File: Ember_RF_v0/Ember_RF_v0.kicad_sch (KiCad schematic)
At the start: 2 parts

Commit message: anything until test launch prep
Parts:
- added JP1: ~, microbuilder:1X20_ROUND, symbol microbuilder:HEADER-1X20ROUND
- added R1, R2, R3: ~, microbuilder:0603, symbol microbuilder:RESISTOR0603
- added R4, R5, R6, R7: 0, microbuilder:0603, symbol microbuilder:RESISTOR0603
- added U3: ~, E22-900M30S:XCVR_E22-900M30S, symbol E22-900M30S:E22-900M30S
- added X1: ~, adafruit:SMA90_DIP, symbol adafruit:SMACONNECTOR
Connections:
- net GPS_RX: now reaches U2.1 (RXD)
- net GPS_RX: now also U1.P$6 (GP4)
- net GND: now reaches U2.12 (GND), U2.3 (GND)
- net GND: now also U1.P$13 (GND), U1.P$18 (GND), U1.P$23 (GND), U1.P$28 (GND), U1.P$3 (GND), U1.P$33 (GND), U1.P$38 (GND), U1.P$8 (GND), JP1.2, R1.1, R2.1, R3.2, U3.1 (GND), U3.11 (GND), U3.12 (GND), U3.2 (GND), U3.20 (GND), U3.22 (GND), U3.3 (GND), U3.4 (GND), U3.5 (GND), X1.GND1, X1.GND2, X1.GND3, X1.GND4
- net SCL: now reaches U2.15 (I2C_SCL)
- net SCL: now also U1.P$5 (GP3), R3.1
- net SDA: now reaches U2.16 (I2C_SDA)
- net SDA: now also U1.P$4 (GP2), R2.2
- net GPS_TX: now reaches U2.2 (TXD)
- net GPS_TX: now also U1.P$7 (GP5)
- net 3v3: now reaches U2.4 (VCC)
- net 3v3: now also U1.P$36 (3V3(OUT)), U3.10 (VCC), U3.9 (VCC)
- net B2B_TX: now reaches U1.P$1 (GP0)
- net B2B_TX: now also JP1.3
- net LORA_MISO: now reaches U1.P$11 (GP8)
- net LORA_MISO: now also R4.1, U3.16 (MISO)
- net LORA_CS: now reaches U1.P$12 (GP9)
- net LORA_CS: now also R1.2, R7.1, U3.19 (NSS)
- net LORA_SCK: now reaches U1.P$14 (GP10)
- net LORA_SCK: now also R6.1, U3.18 (SCK)
- net LORA_MOSI: now reaches U1.P$15 (GP11)
- net LORA_MOSI: now also R5.1, U3.17 (MOSI)
- net LORA_BUSY: now reaches U1.P$16 (GP12)
- net LORA_BUSY: now also U3.14 (BUSY)
- net LORA_RST: now reaches U1.P$17 (GP13)
- net LORA_RST: now also U3.15 (~{RST})
- net LORA_DIO1: now reaches U1.P$19 (GP14)
- net LORA_DIO1: now also U3.13 (DIO1)
- net B2B_RX: now reaches U1.P$2 (GP1)
- net B2B_RX: now also JP1.4
- net 5V: now reaches U1.P$39 (VSYS)
- net 5V: now also JP1.1
- new net: JP1.5, R4.2
- new net: JP1.8, R7.2
- new net: U3.21 (ANT), X1.ANTENNA (ANT)
- new net: JP1.6, R5.2
- new net: JP1.7, R6.2

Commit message: all until 19 mar
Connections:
- net GPS_RESET: now reaches U2.10 (~{RESET})
- net GPS_RESET: now also U1.P$22 (GP17)
- net GPS_WAKE_UP: now reaches U2.7 (WAKE_UP)
- net GPS_WAKE_UP: now also U1.P$21 (GP16)
- net TXEN: now reaches U1.P$10 (GP7)
- net TXEN: now also U3.7 (TXEN)
- net RXEN: now reaches U1.P$9 (GP6)
- net RXEN: now also U3.6 (RXEN)
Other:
- moved on the sheet: R1

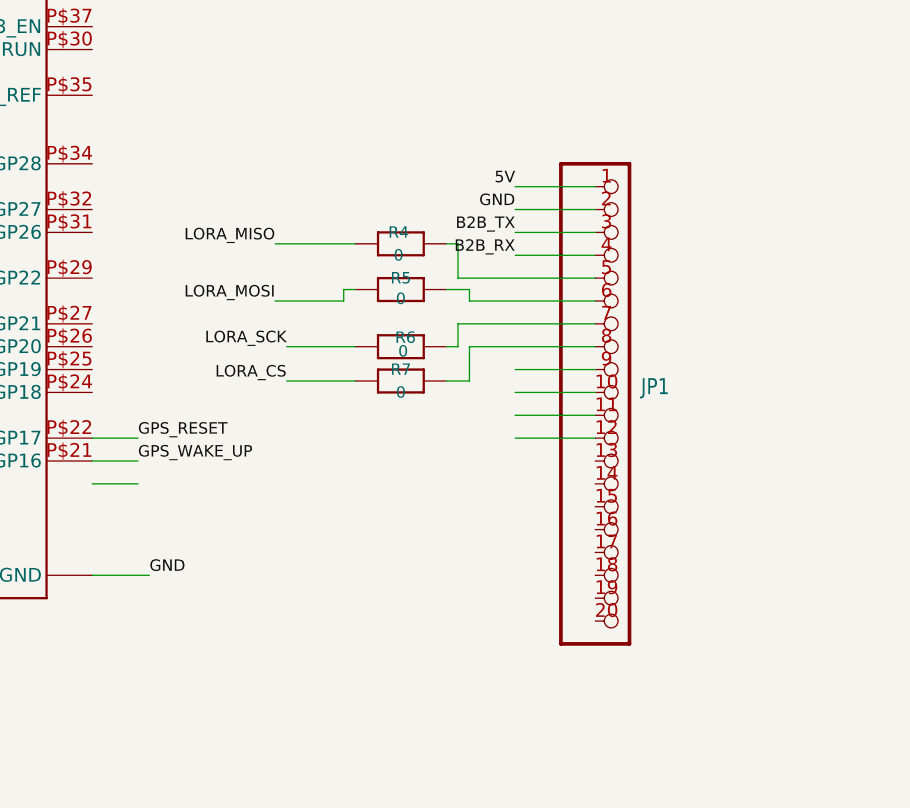
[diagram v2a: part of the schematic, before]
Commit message: Ahaan's RF Headers 16 to 4
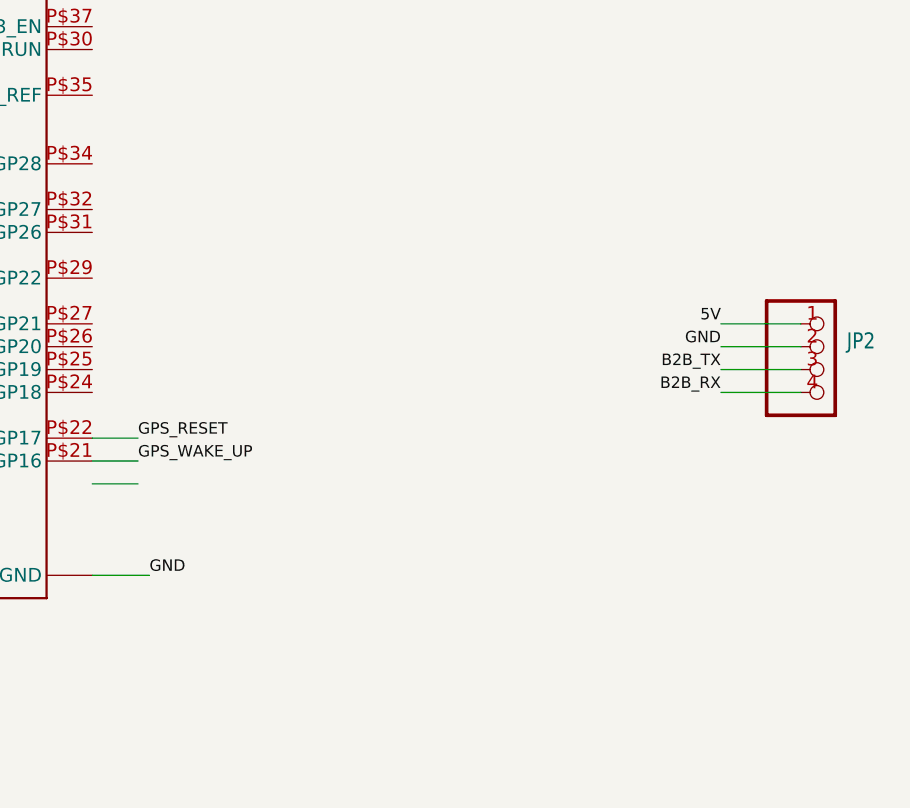
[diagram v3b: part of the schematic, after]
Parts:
- removed JP1: ~, microbuilder:1X20_ROUND, symbol microbuilder:HEADER-1X20ROUND
- removed R4, R5, R6, R7: 0, microbuilder:0603, symbol microbuilder:RESISTOR0603
- added JP2: ~, microbuilder:1X04_OVAL, symbol microbuilder:HEADER-1X4
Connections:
- net 5V: now also JP2.1
- net B2B_RX: now also JP2.4
- net B2B_TX: now also JP2.3
- net GND: now also JP2.2

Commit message: RF Board PCB Attempt 1
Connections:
- no-connect marks 1 -> 24

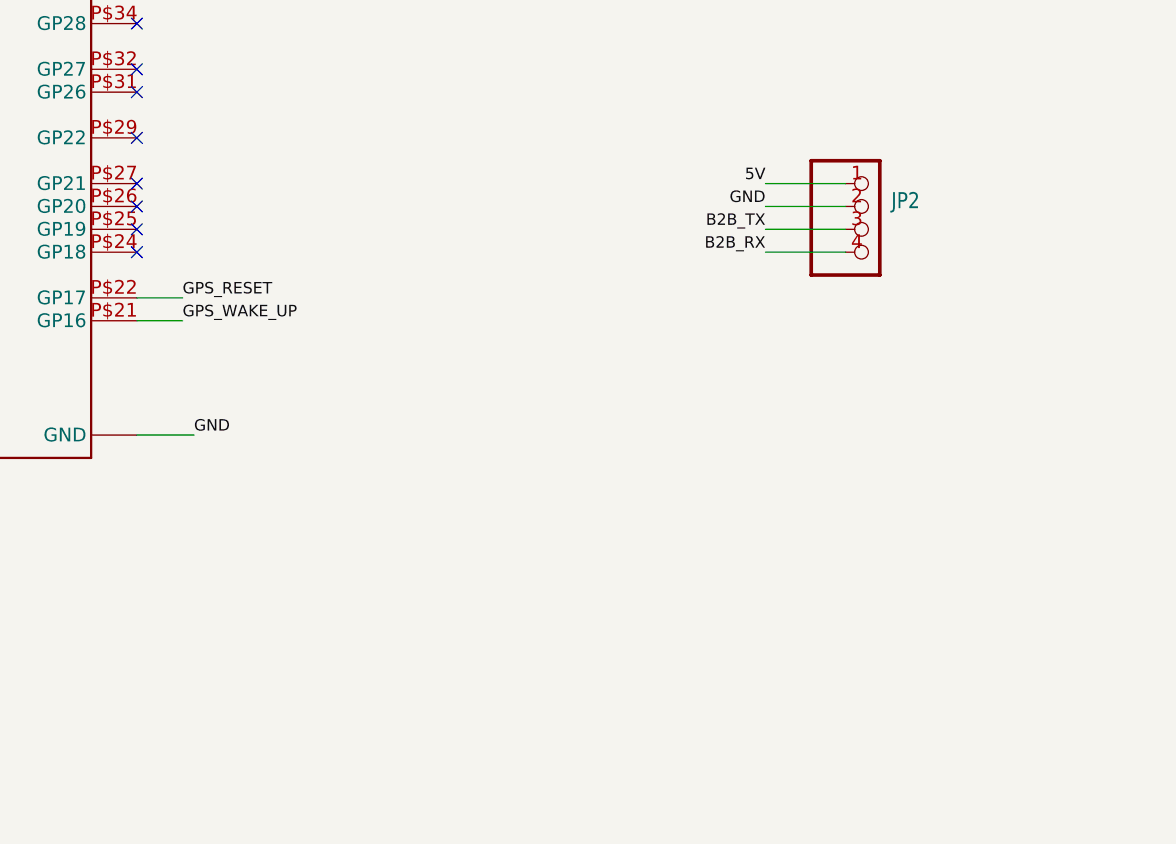
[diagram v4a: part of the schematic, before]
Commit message: Some corrections done and main board routing halfway done
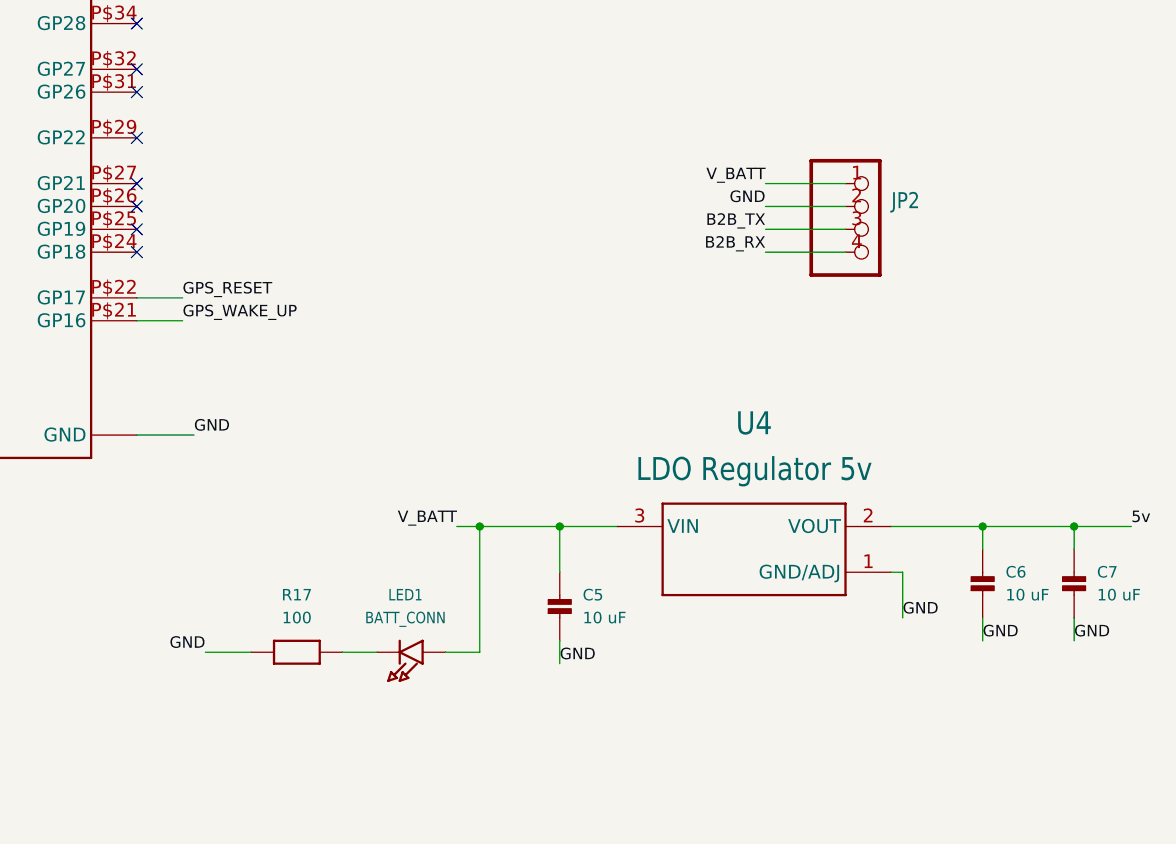
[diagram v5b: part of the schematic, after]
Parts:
- added C5, C6, C7: 10 uF, microbuilder:0603, symbol microbuilder:CAP_CERAMIC0603
- added LED1: BATT_CONN, microbuilder:CHIPLED_0603, symbol microbuilder:LED0603
- added R17: 100, microbuilder:0603, symbol microbuilder:RESISTOR0603
- added U4: LDO Regulator 5v, AMS1117-5.0:SOT229P700X180-4N, symbol AMS1117-5.0:AMS1117-5.0
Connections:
- net 5V: no longer JP2.1
- net GND: now also C5.2 (P$2), C6.2 (P$2), C7.2 (P$2), R17.1, U4.1 (GND/ADJ)
- new net: LED1.C, R17.2
- new net 5v: C6.1 (P$1), C7.1 (P$1), U4.2 (VOUT)
- new net V_BATT: C5.1 (P$1), JP2.1, LED1.A, U4.3 (VIN)

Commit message: All routings completed, Lisan Al-gaib!
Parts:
- removed X1: ~, adafruit:SMA90_DIP, symbol adafruit:SMACONNECTOR
- added J1: ~, sma-connector:RFSOLUTIONS_CON-SMA-EDGE-S, symbol sma-connector:CON-SMA-EDGE-S
- added LS2: BUZZER, CMT-8530S-SMT:CUI_CMT-8530S-SMT, symbol CMT-8530S-SMT:CMT-8530S-SMT
- added Q5: CJ3400, CJ3400:SOT95P240X115-3N, symbol CJ3400:CJ3400
- added R15: 100, microbuilder:0603, symbol microbuilder:RESISTOR0603
- added R27: 1k, microbuilder:0603, symbol microbuilder:RESISTOR0603
- added R4: 33k, microbuilder:0603, symbol microbuilder:RESISTOR0603
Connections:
- net 5V is gone; now on net 5v: U1.P$39 (VSYS)
- net 5v: now also Q5.3 (D)
- net GND: now also J1.G1 (2), J1.G2 (2), J1.G3 (2), J1.G4 (2), R15.2, R4.2
- net at U3.21 (ANT): now also J1.1
- net BUZZER: now reaches U1.P$24 (GP18)
- net BUZZER: now also R27.1
- new net: Q5.1 (G), R27.2, R4.1
- new net: LS2.P, Q5.2 (S)
- new net: LS2.N, R15.1
- no-connect marks 24 -> 23
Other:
- moved on the sheet: R2, R3, U2

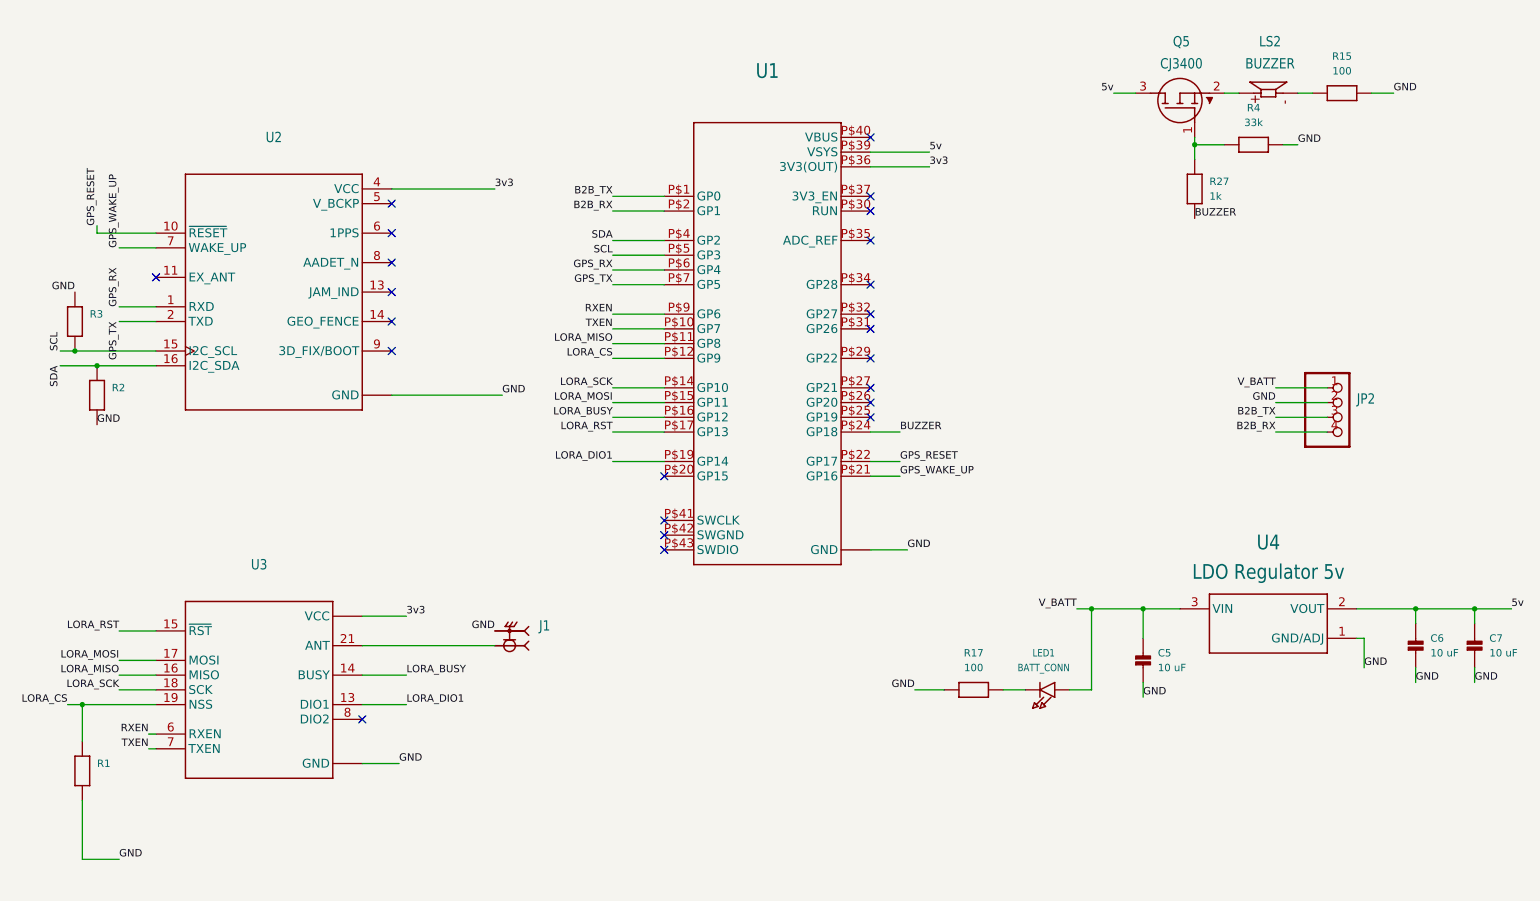
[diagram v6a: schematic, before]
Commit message: TDU board LDO is replaced by AP63205
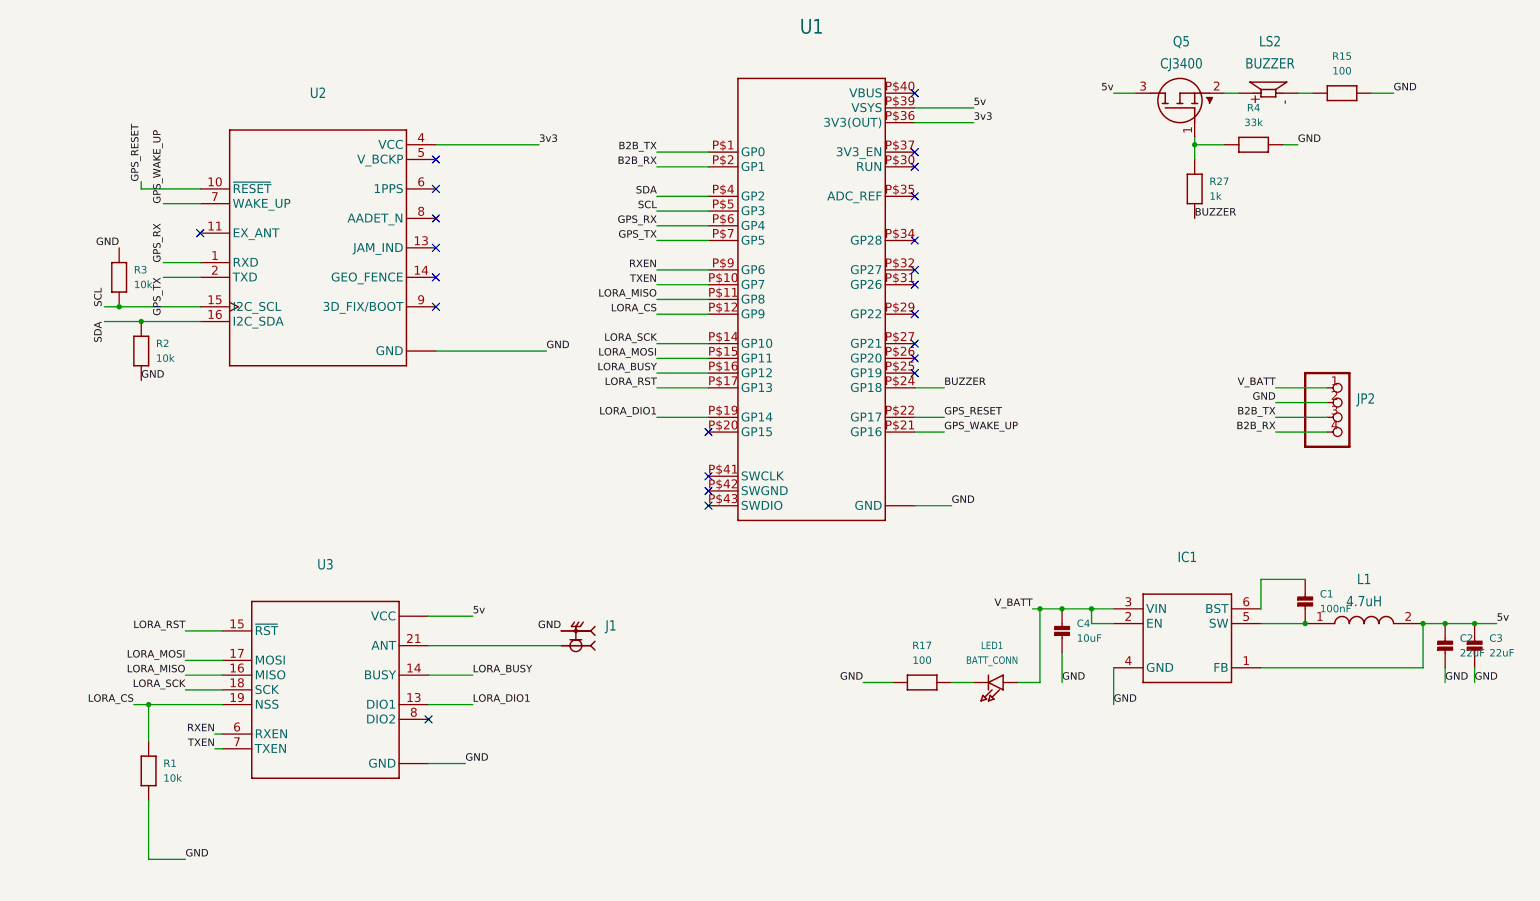
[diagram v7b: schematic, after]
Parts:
- removed C5, C6, C7: 10 uF, microbuilder:0603, symbol microbuilder:CAP_CERAMIC0603
- removed U4: LDO Regulator 5v, AMS1117-5.0:SOT229P700X180-4N, symbol AMS1117-5.0:AMS1117-5.0
- added C1: 100nF, microbuilder:0603, symbol microbuilder:CAP_CERAMIC0603
- added C2, C3: 22uF, microbuilder:0603, symbol microbuilder:CAP_CERAMIC0603
- added C4: 10uF, microbuilder:0603, symbol microbuilder:CAP_CERAMIC0603
- added IC1: ~, AP63205WU-7:SOT95P280X100-6N, symbol AP63205WU-7:AP63205WU-7
- added L1: 4.7uH, SRN3015-4R7M:INDPM3027X150N, symbol SRN3015-4R7M:SRN3015-4R7M
- R1, R2, R3: value ~ -> 10k
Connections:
- net 3v3: no longer U3.10 (VCC), U3.9 (VCC)
- net 5v: now also U3.10 (VCC), U3.9 (VCC), C2.1 (P$1), C3.1 (P$1), IC1.1 (FB), L1.2
- net GND: now also C2.2 (P$2), C3.2 (P$2), C4.2 (P$2), IC1.4 (GND)
- net V_BATT: now also C4.1 (P$1), IC1.2 (EN), IC1.3 (VIN)
- new net: C1.1 (P$1), IC1.6 (BST)
- new net: C1.2 (P$2), IC1.5 (SW), L1.1
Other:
- moved on the sheet: J1, LED1, R1, R17, R2, R3, U1, U2, U3

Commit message: All changes and things are done in both FCU and TDU - Lisan Al-gaib!
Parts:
- added C5: 100nF, microbuilder:0603, symbol microbuilder:CAP_CERAMIC0603
- added JP1: ~, microbuilder:1X02_OVAL, symbol microbuilder:HEADER-1X2
- added Q2: SISA96DN-T1, SISA96DN-T1-GE3:SIS862DNT1GE3, symbol SISA96DN-T1-GE3:SISA96DN-T1-GE3
- added R30: 33k, microbuilder:0603, symbol microbuilder:RESISTOR0603
- added R31: 1k, microbuilder:0603, symbol microbuilder:RESISTOR0603
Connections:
- net 5v: now also C5.2 (P$2), JP1.1
- net GND: now also C5.1 (P$1), Q2.1 (S_1), Q2.2 (S_2), Q2.3 (S_3), R30.2
- net CAM: now reaches U1.P$20 (GP15)
- net CAM: now also R31.1
- new net CAM_GND: JP1.2, Q2.10 (D_6), Q2.11 (D_7), Q2.5 (D_1), Q2.6 (D_2), Q2.7 (D_3), Q2.8 (D_4), Q2.9 (D_5)
- new net G_DROGUE: Q2.4 (G), R30.1, R31.2
- no-connect marks 23 -> 21
